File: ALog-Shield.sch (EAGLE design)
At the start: 32 parts

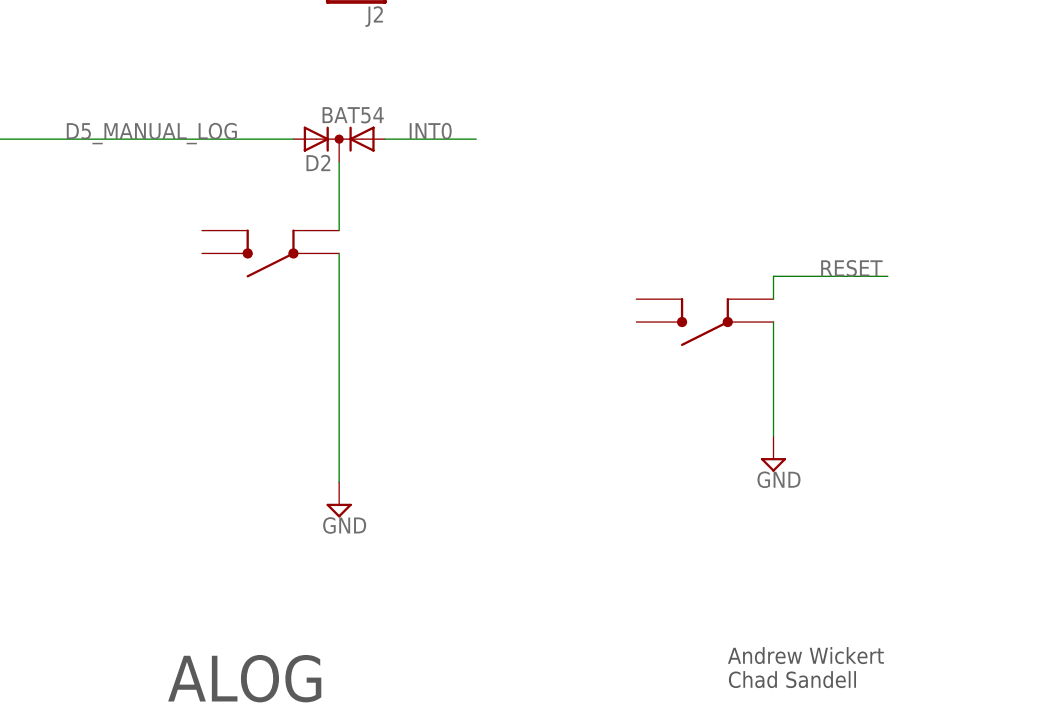
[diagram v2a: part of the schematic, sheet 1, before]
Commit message: Added final Gerbers for Mrk 2.2.1
Cleaned up routing, fixed button issue, generated gerbers for Mrk 2.2.1
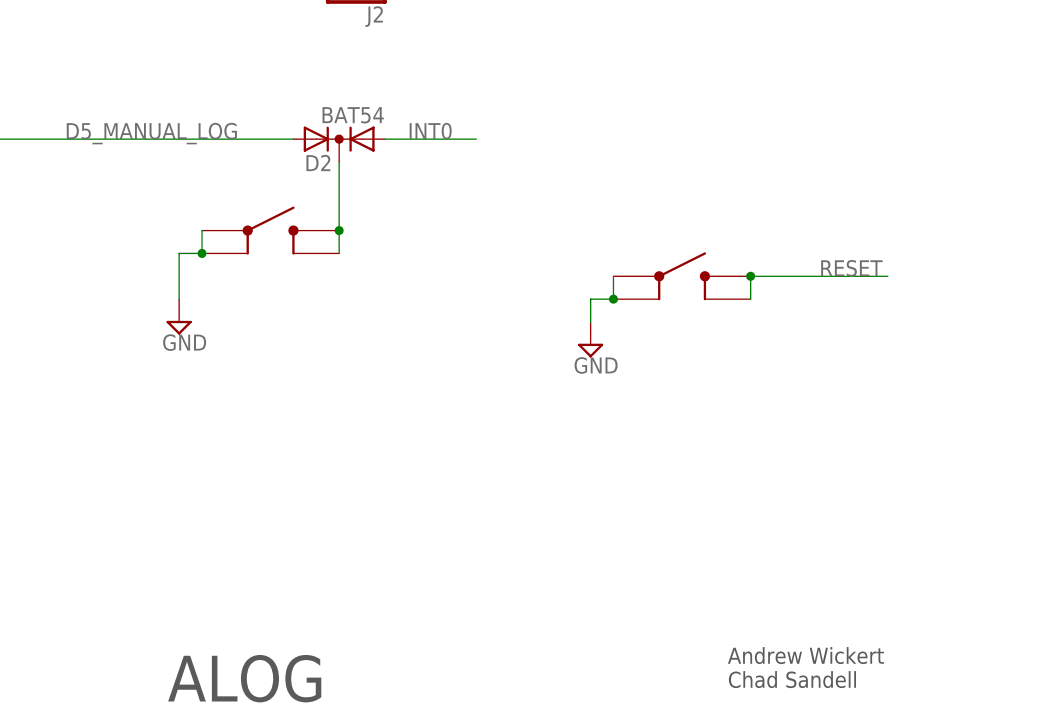
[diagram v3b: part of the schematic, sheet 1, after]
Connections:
- removed net N$11: D2.K, LOG.2
- new net N$1: D2.K, LOG.3, LOG.4
- net GND: now also LOG.2, RESET.2
- net RESET: now also RESET.3, RESET.4; no longer RESET.2
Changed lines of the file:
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@@
 <?xml version="1.0" encoding="utf-8"?>
 <!DOCTYPE eagle SYSTEM "eagle.dtd">
-<eagle version="8.6.0">
+<eagle version="8.5.1">
 <drawing>
 <settings>
@@
 <instance part="SUPPLY40" gate="GND" x="134.62" y="-71.12"/>
 <instance part="+3V5" gate="G$1" x="152.4" y="-60.96"/>
-<instance part="SUPPLY31" gate="GND" x="157.48" y="-195.58"/>
+<instance part="SUPPLY31" gate="GND" x="137.16" y="-182.88"/>
 <instance part="A0" gate="G$1" x="30.48" y="-165.1"/>
 <instance part="A2" gate="G$1" x="30.48" y="-185.42"/>
@@
 <instance part="A1" gate="G$1" x="30.48" y="-175.26"/>
 <instance part="SUPPLY47" gate="GND" x="20.32" y="-177.8"/>
-<instance part="SUPPLY52" gate="GND" x="109.22" y="-200.66"/>
-<instance part="RESET" gate="G$1" x="157.48" y="-180.34" rot="R180"/>
+<instance part="SUPPLY52" gate="GND" x="91.44" y="-180.34"/>
+<instance part="RESET" gate="G$1" x="139.7" y="-175.26"/>
 <instance part="SUPPLY53" gate="GND" x="63.5" y="-208.28"/>
 <instance part="D2" gate="G$1" x="109.22" y="-160.02" rot="R180"/>
-<instance part="LOG" gate="G$1" x="109.22" y="-172.72" rot="R180"/>
+<instance part="LOG" gate="G$1" x="93.98" y="-170.18"/>
 <instance part="FRAME1" gate="G$1" x="0" y="-248.92"/>
 <instance part="FRAME1" gate="G$2" x="83.82" y="-248.92" smashed="yes">
@@
 </segment>
 <segment>
-<wire x1="157.48" y1="-180.34" x2="157.48" y2="-193.04" width="0.1524" layer="91"/>
-<pinref part="SUPPLY31" gate="GND" pin="GND"/>
-<pinref part="RESET" gate="G$1" pin="1"/>
-</segment>
-<segment>
 <pinref part="A3" gate="G$1" pin="1"/>
 <pinref part="SUPPLY42" gate="GND" pin="GND"/>
@@
 <pinref part="SUPPLY47" gate="GND" pin="GND"/>
 <wire x1="20.32" y1="-175.26" x2="25.4" y2="-175.26" width="0.1524" layer="91"/>
-</segment>
-<segment>
-<pinref part="SUPPLY52" gate="GND" pin="GND"/>
-<wire x1="109.22" y1="-172.72" x2="109.22" y2="-198.12" width="0.1524" layer="91"/>
-<pinref part="LOG" gate="G$1" pin="1"/>
 </segment>
 <segment>
@@
 <pinref part="J2" gate="G$1" pin="1"/>
 </segment>
+<segment>
+<pinref part="LOG" gate="G$1" pin="1"/>
+<pinref part="LOG" gate="G$1" pin="2"/>
+<wire x1="93.98" y1="-170.18" x2="93.98" y2="-172.72" width="0.1524" layer="91"/>
+<pinref part="SUPPLY52" gate="GND" pin="GND"/>
+<wire x1="93.98" y1="-172.72" x2="91.44" y2="-172.72" width="0.1524" layer="91"/>
+<wire x1="91.44" y1="-172.72" x2="91.44" y2="-177.8" width="0.1524" layer="91"/>
+<junction x="93.98" y="-172.72"/>
+</segment>
+<segment>
+<pinref part="RESET" gate="G$1" pin="1"/>
+<pinref part="RESET" gate="G$1" pin="2"/>
+<wire x1="139.7" y1="-175.26" x2="139.7" y2="-177.8" width="0.1524" layer="91"/>
+<pinref part="SUPPLY31" gate="GND" pin="GND"/>
+<wire x1="139.7" y1="-177.8" x2="137.16" y2="-177.8" width="0.1524" layer="91"/>
+<wire x1="137.16" y1="-177.8" x2="137.16" y2="-180.34" width="0.1524" layer="91"/>
+<junction x="139.7" y="-177.8"/>
+</segment>
 </net>
 <net name="TX-O" class="0">
@@
 </segment>
 <segment>
-<wire x1="157.48" y1="-175.26" x2="157.48" y2="-177.8" width="0.1524" layer="91"/>
-<wire x1="157.48" y1="-175.26" x2="170.18" y2="-175.26" width="0.1524" layer="91"/>
+<wire x1="154.94" y1="-175.26" x2="170.18" y2="-175.26" width="0.1524" layer="91"/>
 <label x="162.56" y="-175.26" size="1.778" layer="95"/>
-<pinref part="RESET" gate="G$1" pin="2"/>
+<pinref part="RESET" gate="G$1" pin="3"/>
+<pinref part="RESET" gate="G$1" pin="4"/>
+<wire x1="154.94" y1="-175.26" x2="154.94" y2="-177.8" width="0.1524" layer="91"/>
+<junction x="154.94" y="-175.26"/>
 </segment>
 </net>
@@
 </segment>
 </net>
-<net name="N$11" class="0">
-<segment>
-<pinref part="LOG" gate="G$1" pin="2"/>
-<pinref part="D2" gate="G$1" pin="K"/>
-<wire x1="109.22" y1="-170.18" x2="109.22" y2="-162.56" width="0.1524" layer="91"/>
-</segment>
-</net>
 <net name="D4" class="0">
 <segment>
@@
 </segment>
 </net>
+<net name="N$1" class="0">
+<segment>
+<pinref part="D2" gate="G$1" pin="K"/>
+<pinref part="LOG" gate="G$1" pin="3"/>
+<wire x1="109.22" y1="-162.56" x2="109.22" y2="-170.18" width="0.1524" layer="91"/>
+<pinref part="LOG" gate="G$1" pin="4"/>
+<wire x1="109.22" y1="-172.72" x2="109.22" y2="-170.18" width="0.1524" layer="91"/>
+<junction x="109.22" y="-170.18"/>
+</segment>
+</net>
